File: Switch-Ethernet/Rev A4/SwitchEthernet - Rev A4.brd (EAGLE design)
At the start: 86 x 90 mm, 121 parts, among them J1 22-05-7028-02, J2 DF17(4.0)-20DS-0.5V(57), J3 DF17(4.0)-20DP-0.5V(57), P1 RB1-125BAG1A, T1 H1102FNL, T2 H1102FNL, T3 EXMACHINA-LOGO-NAME, U1 TC1264-3.3, U2 TC1264-1.8, U3 KSZ8995MA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

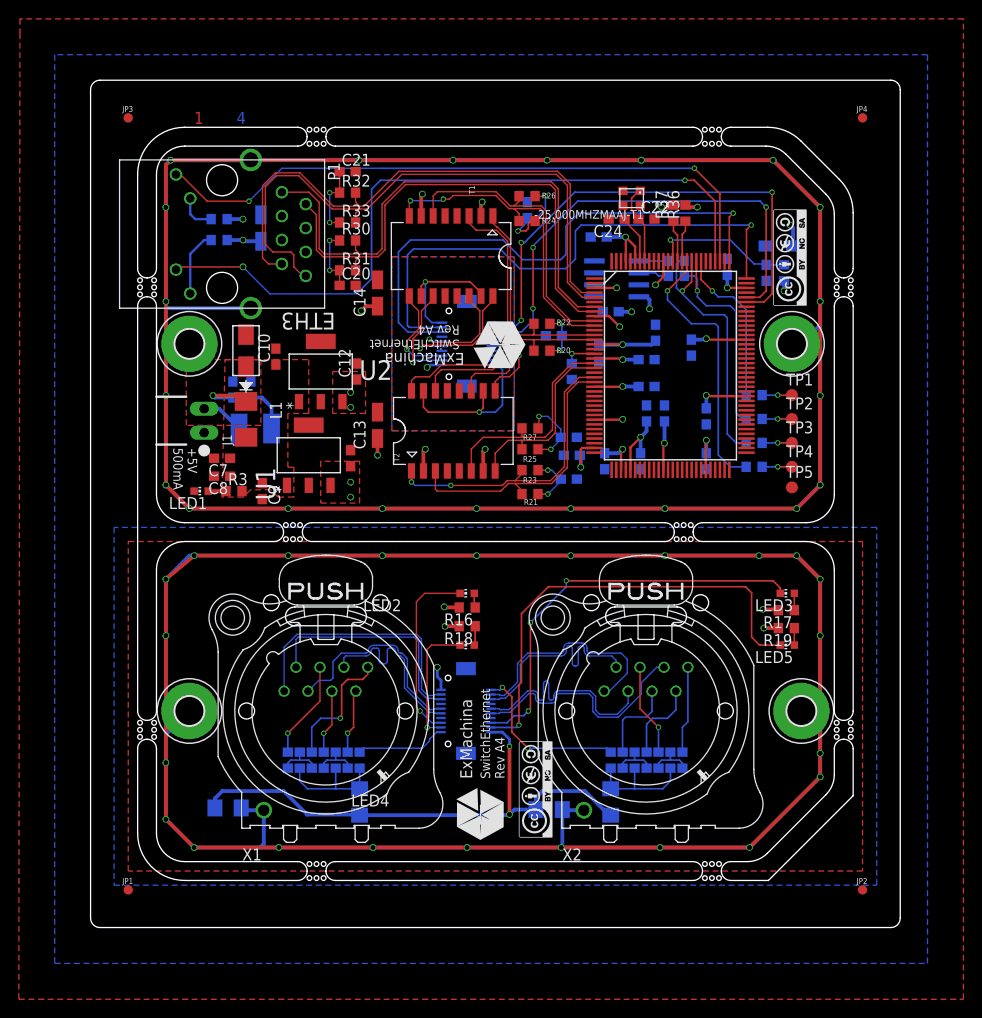
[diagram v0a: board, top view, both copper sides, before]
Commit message: Update libraries and minor tweaks (keepouts)
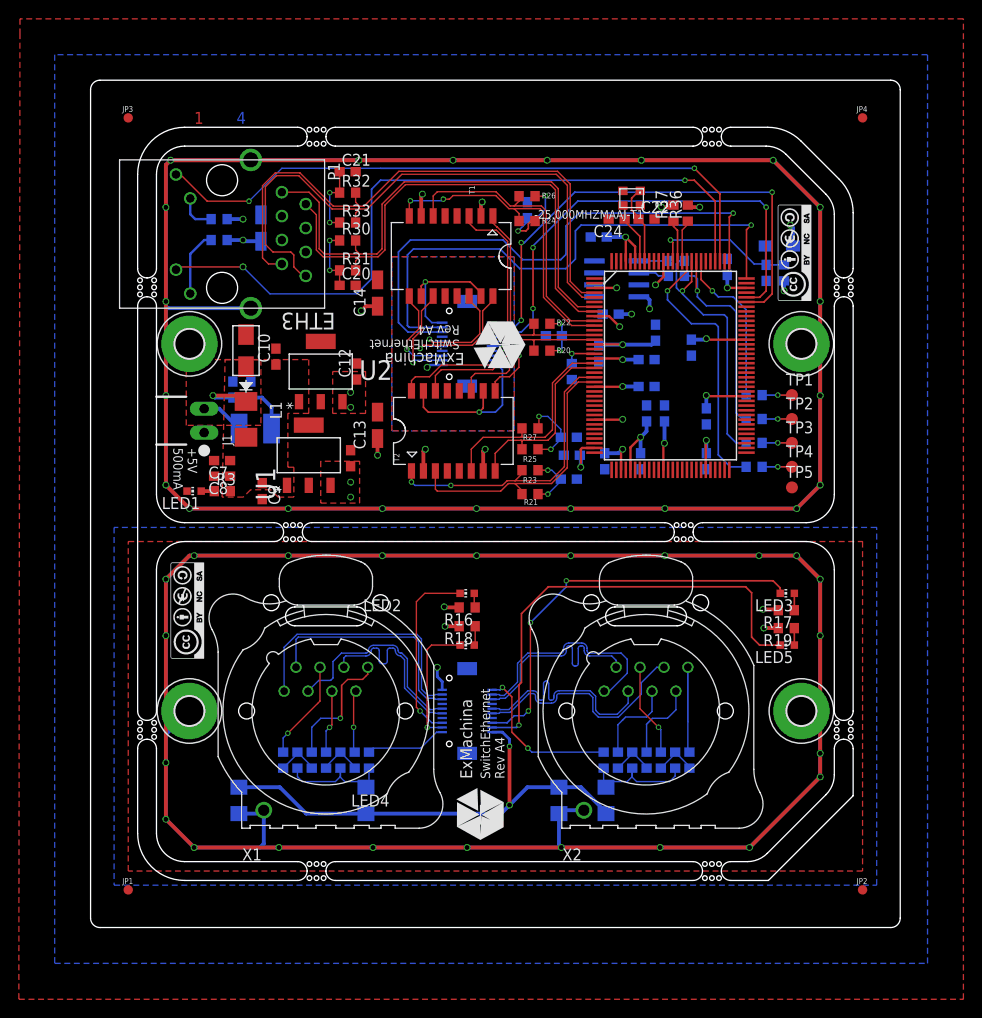
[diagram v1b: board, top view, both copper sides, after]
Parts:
- moved U$2 41.6 mm to (10.3, 33.7)
- moved C2 1.43 mm to (49.8, 13.5), turned to 90 degrees
- moved C1 1.40 mm to (15.8, 13.5), turned to 90 degrees
- moved R3 1.25 mm to (14.0, 46.4)
- moved MP3 1.00 mm to (75.5, 62.0)
- moved R15 1.00 mm to (29.6, 17.8)
- moved LED1 0.75 mm to (11.0, 46.4)
- moved R14 0.75 mm to (54.5, 17.8)
- moved R4 0.75 mm to (63.6, 17.8)
- moved R9 0.75 mm to (28.1, 17.8)
- moved U$3 0.71 mm to (74.8, 71.7)
- moved C6 0.69 mm to (29.2, 13.5)
- moved C5 0.52 mm to (54.8, 13.5)
- moved R1 0.50 mm to (20.5, 17.8)
- moved R10 0.50 mm to (56.0, 17.8)
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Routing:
- net GND: track 57.7 -> 51.7 mm
- net CT_1: track 23.8 -> 22.8 mm
- net CT_2: track 36.1 -> 35.1 mm
- net N$32: track 12.5 -> 13.2 mm
- net N$13: track 12.5 -> 13.1 mm
- net N$23: track 1.89 -> 1.39 mm

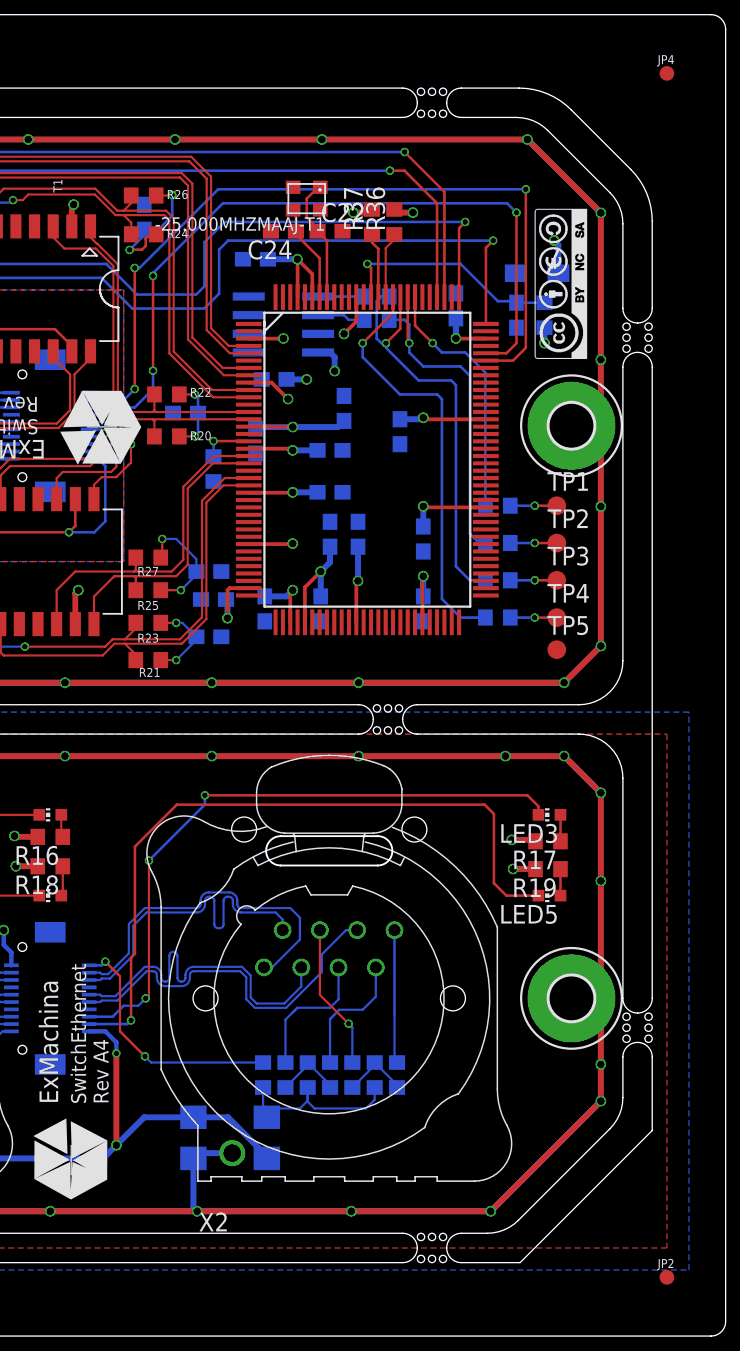
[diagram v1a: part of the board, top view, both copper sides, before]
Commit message: Fixed missing connection to GND
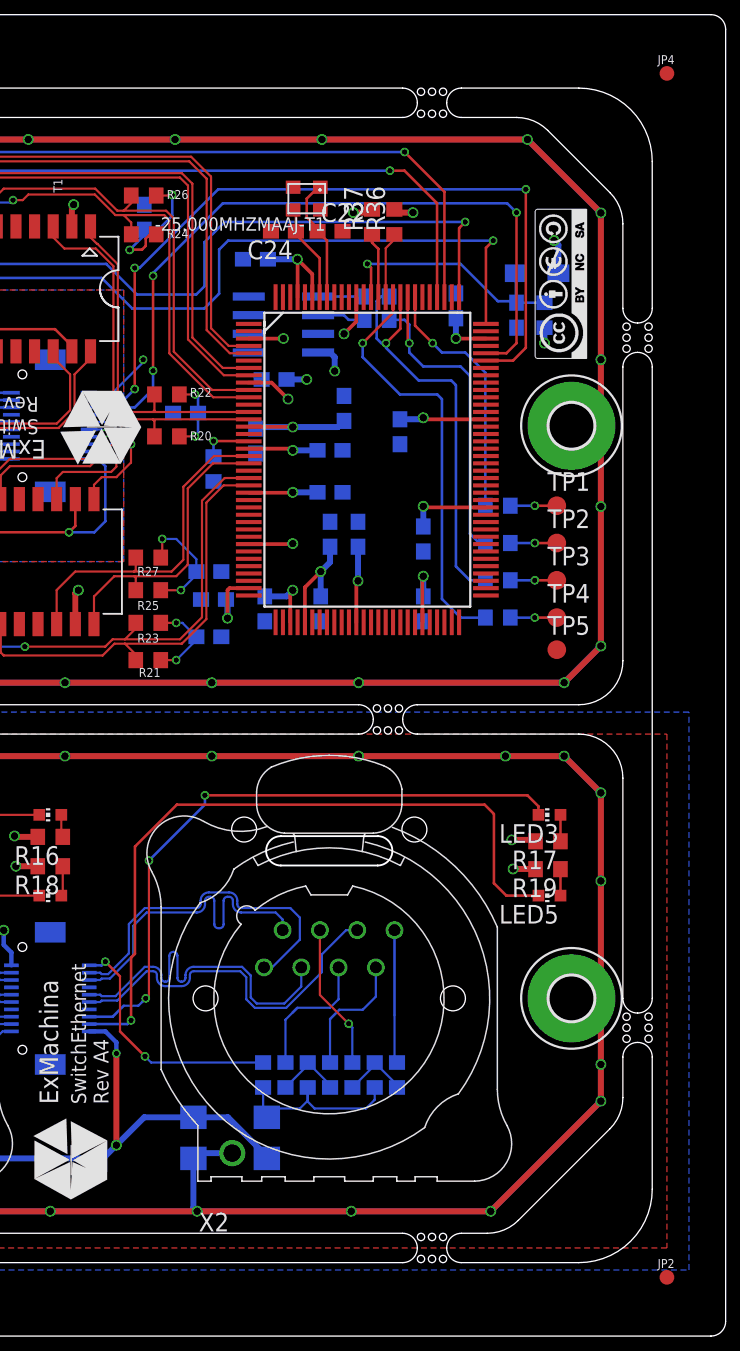
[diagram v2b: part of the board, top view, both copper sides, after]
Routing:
- net GND: track 51.7 -> 56.4 mm, vias 2 -> 3
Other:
- outline, holes or cut-outs redrawn
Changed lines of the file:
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@@
 <layers>
 <layer number="1" name="Top" color="16" fill="1" visible="yes" active="yes"/>
-<layer number="2" name="Route2" color="17" fill="1" visible="no" active="yes"/>
-<layer number="3" name="Route3" color="4" fill="3" visible="yes" active="yes"/>
+<layer number="2" name="Route2" color="17" fill="1" visible="yes" active="yes"/>
+<layer number="3" name="Route3" color="4" fill="3" visible="no" active="yes"/>
 <layer number="14" name="Route14" color="1" fill="6" visible="no" active="no"/>
 <layer number="15" name="Route15" color="19" fill="1" visible="yes" active="yes"/>
@@
 <layer number="23" name="tOrigins" color="15" fill="1" visible="yes" active="yes"/>
 <layer number="24" name="bOrigins" color="15" fill="1" visible="yes" active="yes"/>
-<layer number="25" name="tNames" color="55" fill="1" visible="no" active="yes"/>
+<layer number="25" name="tNames" color="55" fill="1" visible="yes" active="yes"/>
 <layer number="26" name="bNames" color="54" fill="1" visible="yes" active="yes"/>
-<layer number="27" name="tValues" color="53" fill="1" visible="no" active="yes"/>
+<layer number="27" name="tValues" color="53" fill="1" visible="yes" active="yes"/>
 <layer number="28" name="bValues" color="52" fill="1" visible="yes" active="yes"/>
 <layer number="29" name="tStop" color="7" fill="3" visible="no" active="yes"/>
@@
 <layer number="39" name="tKeepout" color="4" fill="1" visible="yes" active="yes"/>
 <layer number="40" name="bKeepout" color="3" fill="1" visible="yes" active="yes"/>
-<layer number="41" name="tRestrict" color="4" fill="10" visible="yes" active="yes"/>
-<layer number="42" name="bRestrict" color="3" fill="10" visible="yes" active="yes"/>
+<layer number="41" name="tRestrict" color="4" fill="10" visible="no" active="yes"/>
+<layer number="42" name="bRestrict" color="3" fill="10" visible="no" active="yes"/>
 <layer number="43" name="vRestrict" color="2" fill="10" visible="no" active="yes"/>
 <layer number="44" name="Drills" color="16" fill="1" visible="no" active="yes"/>
@@
 <layer number="49" name="Reference" color="48" fill="1" visible="no" active="yes"/>
 <layer number="50" name="dxf" color="7" fill="1" visible="no" active="yes"/>
-<layer number="51" name="tDocu" color="55" fill="1" visible="no" active="yes"/>
+<layer number="51" name="tDocu" color="55" fill="1" visible="yes" active="yes"/>
 <layer number="52" name="bDocu" color="54" fill="1" visible="yes" active="yes"/>
 <layer number="91" name="Nets" color="2" fill="1" visible="no" active="no"/>
@@
 <board>
 <plain>
-<wire x1="79" y1="19" x2="79" y2="16.242640625" width="0" layer="20"/>
-<wire x1="79" y1="16.242640625" x2="78.121321875" y2="14.121321875" width="0" layer="20" curve="-44.999958"/>
-<wire x1="78.121321875" y1="14.121321875" x2="71.878678125" y2="7.878678125" width="0" layer="20"/>
-<wire x1="71.878678125" y1="7.878678125" x2="69.757359375" y2="7" width="0" layer="20" curve="-44.99994"/>
-<wire x1="69.757359375" y1="7" x2="68" y2="7" width="0" layer="20"/>
+<wire x1="68" y1="7" x2="69.757359375" y2="7" width="0" layer="20"/>
+<wire x1="69.757359375" y1="7" x2="71.878678125" y2="7.878678125" width="0" layer="20" curve="44.999958"/>
+<wire x1="71.878678125" y1="7.878678125" x2="78.121321875" y2="14.121321875" width="0" layer="20"/>
+<wire x1="78.121321875" y1="14.121321875" x2="79" y2="16.242640625" width="0" layer="20" curve="44.99994"/>
+<wire x1="79" y1="16.242640625" x2="79" y2="19" width="0" layer="20"/>
 <wire x1="68" y1="7" x2="67" y2="6" width="0" layer="20" curve="90"/>
 <wire x1="64" y1="7" x2="26" y2="7" width="0" layer="20"/>
@@
 <wire x1="7" y1="10" x2="7" y2="19" width="0" layer="20"/>
 <wire x1="22" y1="7" x2="23" y2="6" width="0" layer="20" curve="-90"/>
+<wire x1="5" y1="19" x2="5" y2="10" width="0" layer="20"/>
+<wire x1="5" y1="10" x2="10" y2="5" width="0" layer="20" curve="90"/>
 <wire x1="10" y1="5" x2="22" y2="5" width="0" layer="20"/>
 <wire x1="22" y1="5" x2="23" y2="6" width="0" layer="20" curve="90"/>
@@
 <wire x1="7" y1="19" x2="6" y2="20" width="0" layer="20" curve="90"/>
 <wire x1="6" y1="20" x2="5" y2="19" width="0" layer="20" curve="90"/>
-<wire x1="5" y1="19" x2="5" y2="10" width="0" layer="20"/>
 <wire x1="65" y1="43" x2="76" y2="43" width="0" layer="20"/>
 <wire x1="76" y1="43" x2="79" y2="46" width="0" layer="20" curve="90"/>
@@
 <wire x1="79" y1="75.757359375" x2="78.121321875" y2="77.878678125" width="0" layer="20" curve="44.999958"/>
 <wire x1="78.121321875" y1="77.878678125" x2="73.878678125" y2="82.121321875" width="0" layer="20"/>
+<wire x1="73.878678125" y1="82.121321875" x2="71.757359375" y2="83" width="0" layer="20" curve="44.99994"/>
+<wire x1="71.757359375" y1="83" x2="68" y2="83" width="0" layer="20"/>
 <wire x1="79" y1="70" x2="80" y2="69" width="0" layer="20" curve="90"/>
 <wire x1="80" y1="69" x2="81" y2="70" width="0" layer="20" curve="90"/>
-<wire x1="75.464465625" y1="83.535534375" x2="79.535534375" y2="79.464465625" width="0" layer="20"/>
-<wire x1="79.535534375" y1="79.464465625" x2="81" y2="75.92893125" width="0" layer="20" curve="-45"/>
-<wire x1="81" y1="75.92893125" x2="81" y2="70" width="0" layer="20"/>
+<wire x1="68" y1="85" x2="76" y2="85" width="0" layer="20"/>
+<wire x1="76" y1="85" x2="81" y2="80" width="0" layer="20" curve="-90"/>
+<wire x1="81" y1="80" x2="81" y2="70" width="0" layer="20"/>
+<wire x1="22" y1="85" x2="10" y2="85" width="0" layer="20"/>
+<wire x1="10" y1="85" x2="5" y2="80" width="0" layer="20" curve="90"/>
 <wire x1="5" y1="80" x2="5" y2="70" width="0" layer="20"/>
 <wire x1="5" y1="70" x2="6" y2="69" width="0" layer="20" curve="90"/>
@@
 <wire x1="7" y1="80" x2="7" y2="70" width="0" layer="20"/>
 <wire x1="7" y1="66" x2="6" y2="67" width="0" layer="20" curve="90"/>
-<wire x1="73.878678125" y1="82.121321875" x2="71.757359375" y2="83" width="0" layer="20" curve="44.99994"/>
-<wire x1="71.757359375" y1="83" x2="68" y2="83" width="0" layer="20"/>
 <wire x1="68" y1="83" x2="67" y2="84" width="0" layer="20" curve="-90"/>
-<wire x1="68" y1="85" x2="71.92893125" y2="85" width="0" layer="20"/>
-<wire x1="71.92893125" y1="85" x2="75.464465625" y2="83.535534375" width="0" layer="20" curve="-45"/>
 <wire x1="68" y1="85" x2="67" y2="84" width="0" layer="20" curve="90"/>
 <wire x1="65" y1="84" x2="64" y2="83" width="0" layer="20" curve="-90"/>
@@
 <wire x1="26" y1="83" x2="25" y2="84" width="0" layer="20" curve="-90"/>
 <wire x1="23" y1="84" x2="22" y2="85" width="0" layer="20" curve="90"/>
-<wire x1="22" y1="85" x2="10" y2="85" width="0" layer="20"/>
 <wire x1="23" y1="84" x2="22" y2="83" width="0" layer="20" curve="-90"/>
 <text x="43.965" y="15.795" size="1.016" layer="21" rot="R90">SwitchEthernet
@@
 <text x="68.96" y="74.59" size="0.8128" layer="22" rot="SMR180" align="center-left">+1V8</text>
 <wire x1="6" y1="67" x2="5" y2="66" width="0" layer="20" curve="90"/>
-<wire x1="5" y1="10" x2="10" y2="5" width="0" layer="20" curve="90"/>
 <wire x1="67" y1="6" x2="68" y2="5" width="0" layer="20" curve="90"/>
-<wire x1="68" y1="5" x2="72" y2="5" width="0" layer="20"/>
-<wire x1="81" y1="14" x2="81" y2="19" width="0" layer="20"/>
+<wire x1="81" y1="19" x2="81" y2="10" width="0" layer="20"/>
+<wire x1="81" y1="10" x2="76" y2="5" width="0" layer="20" curve="-90"/>
+<wire x1="76" y1="5" x2="68" y2="5" width="0" layer="20"/>
 <wire x1="81" y1="19" x2="80" y2="20" width="0" layer="20" curve="90"/>
 <wire x1="25" y1="84" x2="26" y2="85" width="0" layer="20" curve="-90"/>
 <wire x1="26" y1="85" x2="64" y2="85" width="0" layer="20"/>
 <wire x1="64" y1="85" x2="65" y2="84" width="0" layer="20" curve="-90"/>
-<wire x1="10" y1="85" x2="5" y2="80" width="0" layer="20" curve="90"/>
 <wire x1="0" y1="1" x2="0" y2="89" width="0" layer="20"/>
 <wire x1="0" y1="89" x2="1" y2="90" width="0" layer="20" curve="-90"/>
@@
 <text x="8.785" y="50.955" size="1.016" layer="21" rot="SR270">+5V
 500mA</text>
-<wire x1="81" y1="14" x2="72" y2="5" width="0" layer="20"/>
 </plain>
 <attributes>
@@
 <wire x1="44.5" y1="13" x2="46.4" y2="14.9" width="0.4064" layer="16"/>
 <wire x1="46.4" y1="14.9" x2="49.75" y2="14.9" width="0.4064" layer="16"/>
-<wire x1="48.3625" y1="62.865" x2="42.65" y2="64.25" width="0" layer="19" extent="16-16"/>
-<wire x1="43.75" y1="20.75" x2="51.65" y2="47.625" width="0" layer="19" extent="16-16"/>
+<wire x1="42.65" y1="64.25" x2="44.25" y2="64.25" width="0.15" layer="16"/>
+<via x="46.325" y="66.5" extent="1-16" drill="0.35"/>
+<wire x1="44.25" y1="64.25" x2="46.325" y2="66.325" width="0.15" layer="16"/>
+<wire x1="46.325" y1="66.325" x2="46.325" y2="66.5" width="0.15" layer="16"/>
+<wire x1="51.65" y1="47.625" x2="43.75" y2="20.75" width="0" layer="19" extent="16-16"/>
 </signal>
 <signal name="L3-1">
